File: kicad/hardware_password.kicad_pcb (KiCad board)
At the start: 2 copper layers, 7 parts, among them J1 Conn_01x04_Socket, J2 Conn_01x06_Socket, SW1 SW_MEC_5E, SW2 SW_MEC_5E, SW3 SW_MEC_5E, SW4 SW_MEC_5E

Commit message: Add files via upload
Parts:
- removed A1: Adafruit_Feather_HUZZAH32_ESP32, Module:Adafruit_Feather
- added C1: 100pF, 0.1nF, Capacitor_SMD:C_0805_2012Metric, F.Cu at (93.1, 156.3)
- added U1: ESP32-S3-DEVKITC-1-N8R2, ESP32-S3-DEVKITC-1-N8R2:XCVR_ESP32-S3-DEVKITC-1-N8R2, F.Cu at (113.6, 135.4)
- J1: footprint D01_9970442:HARWIN_D01-9970442 -> PPTC041LFBN_RC:SULLINS_PPTC041LFBN-RC
- J2: footprint PPTC061LFBN_RC (1):SULLINS_PPTC061LFBN-RC -> PPTC061LFBN_RC(1):SULLINS_PPTC061LFBN-RC
- SW1, SW2, SW3, SW4: value SW_MEC_5E -> B3F-1020; footprint D01_9970442:HARWIN_D01-9970442 -> b3f-1020:SW_B3F-1000_OMR
- moved SW3 84.9 mm to (99.2, 70.6)
- moved SW2 82.2 mm to (110.2, 58.6)
- moved SW1 72.4 mm to (121.2, 70.6)
- moved SW4 71.1 mm to (110.2, 82.1)
- moved J1 39.9 mm to (135.1, 151.5), turned to -90 degrees
- moved J2 28.9 mm to (135.1, 114.5), turned to 90 degrees
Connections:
- net /IO32 renamed /IO10
- net /IO33 renamed /IO13
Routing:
- net GND: track 158.8 -> 1.79 mm, vias 0 -> 1
- net /5V: track 79.0 -> 0.03 mm
- net /IO14: track 28.4 -> 97.9 mm
- net /IO10: track 31.2 -> 94.8 mm
- net /IO13: track 37.2 -> 78.9 mm
- net /IO15: track 33.0 -> 61.8 mm
- net /MISO: track 32.9 -> 10.2 mm
- net /MOSI: track 29.4 -> 10.2 mm
- net /SCK: track 25.7 -> 10.2 mm
- net /CS: track 21.1 -> 10.2 mm
- net /SDA: track 45.4 -> 52.0 mm
- added copper zone on F.Cu, net /5V
- added copper zone on In1.Cu, net GND
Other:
- board outline added: 51 x 113 mm
- copper layers 2 -> 4
- board text added: "Team #15, Ver 1.0 11/15/2024"

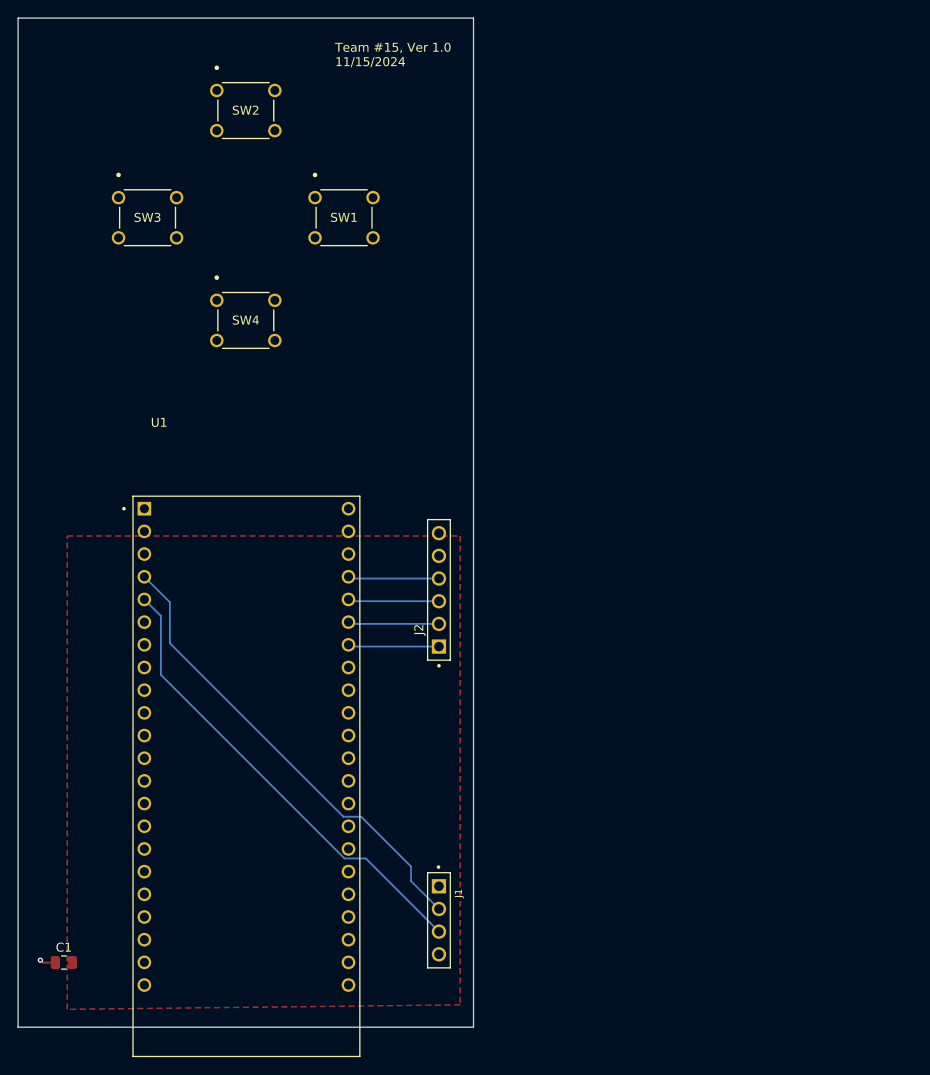
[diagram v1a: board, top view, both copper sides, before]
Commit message: moved power planes to inner layers
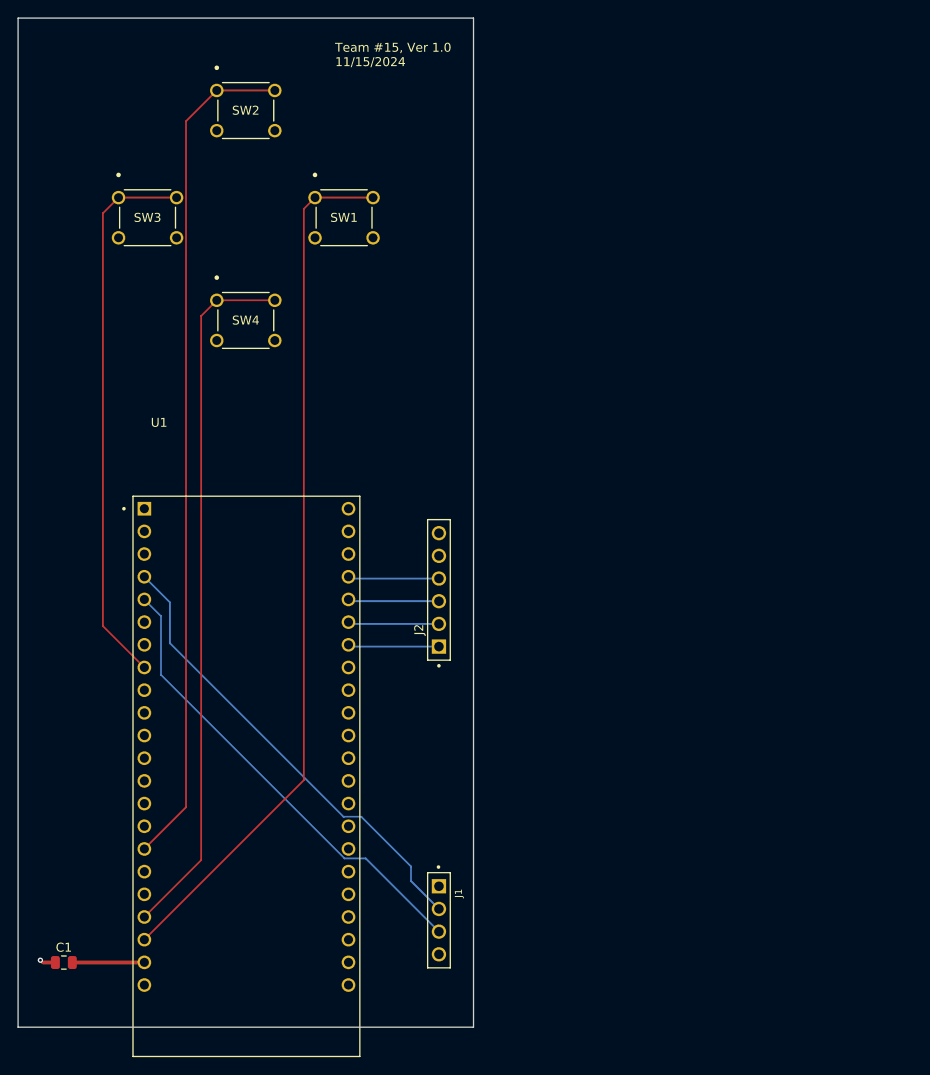
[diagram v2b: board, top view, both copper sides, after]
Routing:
- net /5V: track 0.03 -> 8.07 mm
- added copper zone on In2.Cu, net /5V
- removed copper zone on F.Cu, net /5V
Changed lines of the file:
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@@
+	)
+	(segment
+		(start 94.0782 156.259)
+		(end 102.121 156.259)
+		(width 0.4)
+		(layer "F.Cu")
+		(net 1)
 	)
 	(segment
@@
 		(start 90.759 156.259)
 		(end 92.1782 156.259)
-		(width 0.2)
+		(width 0.4)
 		(layer "F.Cu")
 		(net 2)
@@
 		(end 102.14 153.7)
 		(width 0.2)
-		(layer "In2.Cu")
+		(layer "F.Cu")
+		(net 9)
+	)
+	(segment
+		(start 120 71.854899)
+		(end 120 135.84)
+		(width 0.2)
+		(layer "F.Cu")
+		(net 9)
+	)
+	(segment
+		(start 127.750001 70.6049)
+		(end 121.249999 70.6049)
+		(width 0.2)
+		(layer "F.Cu")
+		(net 9)
+	)
+	(segment
+		(start 121.249999 70.6049)
+		(end 120 71.854899)
+		(width 0.2)
+		(layer "F.Cu")
 		(net 9)
 	)
@@
 	)
 	(segment
-		(start 120 71.854899)
-		(end 120 135.84)
-		(width 0.2)
-		(layer "In2.Cu")
-		(net 9)
-	)
-	(segment
-		(start 127.750001 70.6049)
-		(end 121.249999 70.6049)
-		(width 0.2)
-		(layer "In2.Cu")
-		(net 9)
-	)
-	(segment
-		(start 121.249999 70.6049)
-		(end 120 71.854899)
-		(width 0.2)
-		(layer "In2.Cu")
-		(net 9)
-	)
-	(segment
 		(start 121.249999 70.6049)
 		(end 121.1049 70.6049)
@@
 		(end 102.14 143.54)
 		(width 0.2)
-		(layer "In2.Cu")
+		(layer "F.Cu")
 		(net 10)
 	)
@@
 		(end 110.249999 58.6049)
 		(width 0.2)
-		(layer "In2.Cu")
+		(layer "F.Cu")
 		(net 10)
 	)
@@
 		(end 106.804 62.050899)
 		(width 0.2)
-		(layer "In2.Cu")
+		(layer "F.Cu")
 		(net 10)
 	)
@@
 		(end 106.804 138.876)
 		(width 0.2)
-		(layer "In2.Cu")
+		(layer "F.Cu")
 		(net 10)
 	)
@@
 		(end 97.5 72.354899)
 		(width 0.2)
-		(layer "In2.Cu")
+		(layer "F.Cu")
 		(net 11)
 	)
@@
 		(end 97.5 118.58)
 		(width 0.2)
-		(layer "In2.Cu")
+		(layer "F.Cu")
 		(net 11)
 	)
@@
 		(end 102.14 123.22)
 		(width 0.2)
-		(layer "In2.Cu")
+		(layer "F.Cu")
 		(net 11)
 	)
@@
 		(end 99.249999 70.6049)
 		(width 0.2)
-		(layer "In2.Cu")
+		(layer "F.Cu")
 		(net 11)
 	)
@@
 		(end 102.14 151.16)
 		(width 0.2)
-		(layer "In2.Cu")
+		(layer "F.Cu")
 		(net 12)
 	)
@@
 		(end 110.249999 82.1049)
 		(width 0.2)
-		(layer "In2.Cu")
+		(layer "F.Cu")
 		(net 12)
 	)
@@
 		(end 108.5 83.854899)
 		(width 0.2)
-		(layer "In2.Cu")
+		(layer "F.Cu")
 		(net 12)
 	)
@@
 		(end 108.5 144.8)
 		(width 0.2)
-		(layer "In2.Cu")
+		(layer "F.Cu")
 		(net 12)
-	)
-	(zone
-		(net 1)
-		(net_name "/5V")
-		(layer "F.Cu")
-		(hatch edge 0.5)
-		(priority 1)
-		(connect_pads
-			(clearance 0.5)
-		)
-		(min_thickness 0.25)
-		(filled_areas_thickness no)
-		(fill yes
-			(thermal_gap 0.5)
-			(thermal_bridge_width 0.5)
-			(smoothing fillet)
-			(radius 1)
-		)
-		(polygon
-			(pts
-				(xy 137.5 108.5) (xy 137.5 161) (xy 93.5 161.5) (xy 93.5 108.5)
-			)
-		)
 	)
 	(zone
@@
 			(thermal_bridge_width 0.5)
 			(smoothing fillet)
-			(radius 1)
+			(radius 3)
 		)
 		(polygon
@@
 			)
 		)
+	)
+	(zone
+		(net 1)
+		(net_name "/5V")
+		(layer "In2.Cu")
+		(hatch edge 0.5)
+		(priority 1)
+		(connect_pads
+			(clearance 0.5)
+		)
+		(min_thickness 0.25)
+		(filled_areas_thickness no)
+		(fill yes
+			(thermal_gap 0.5)
+			(thermal_bridge_width 0.5)
+			(smoothing fillet)
+			(radius 3)
+		)
+		(polygon
+			(pts
+				(xy 137.5 108.5) (xy 137.5 161) (xy 93.5 161.5) (xy 93.5 108.5)
+			)
+		)
